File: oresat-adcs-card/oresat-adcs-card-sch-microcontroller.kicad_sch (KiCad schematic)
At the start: 29 parts, among them J2 ORESAT-DEBUG-CONNECTOR-SOLAR, U14 TCAN330GDCNT, U15 STM32F042K6T7, X2 ECS-160-10-36Q-ES-TR

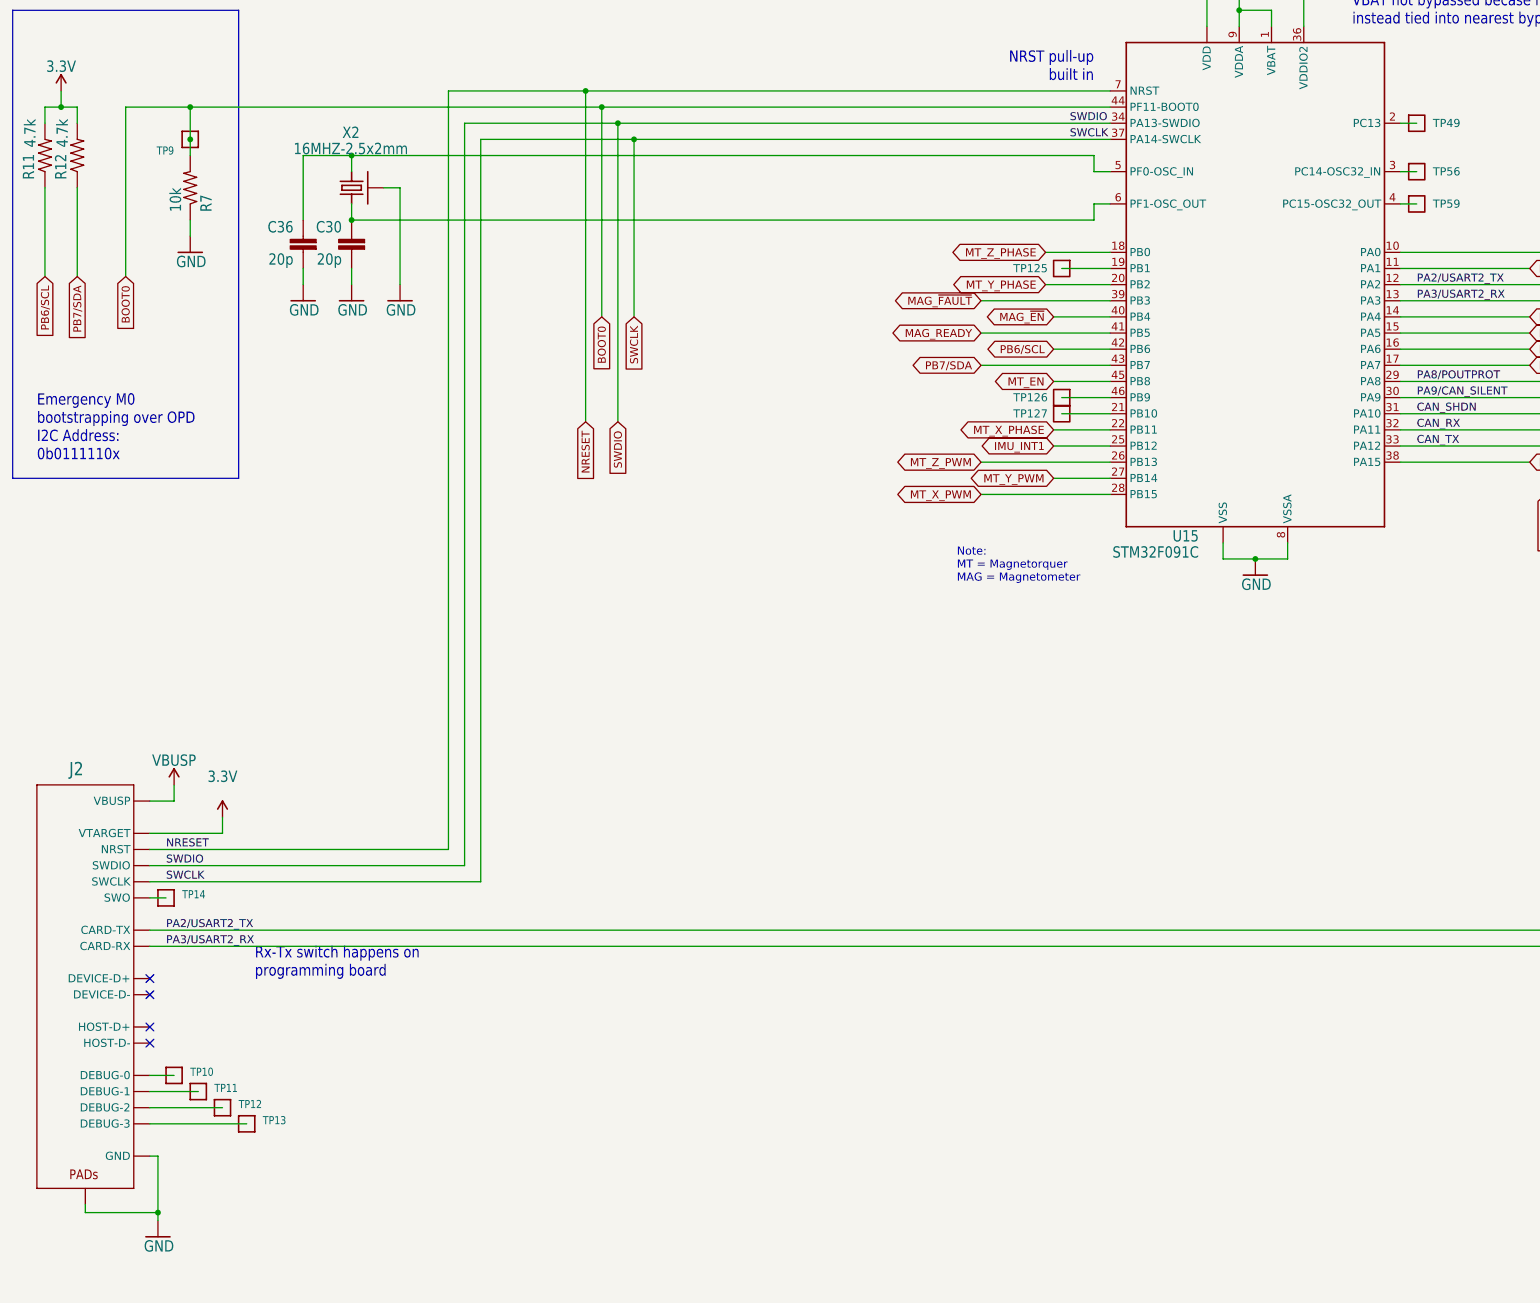
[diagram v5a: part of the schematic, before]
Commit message: Updated ADCS card and fixed library issues
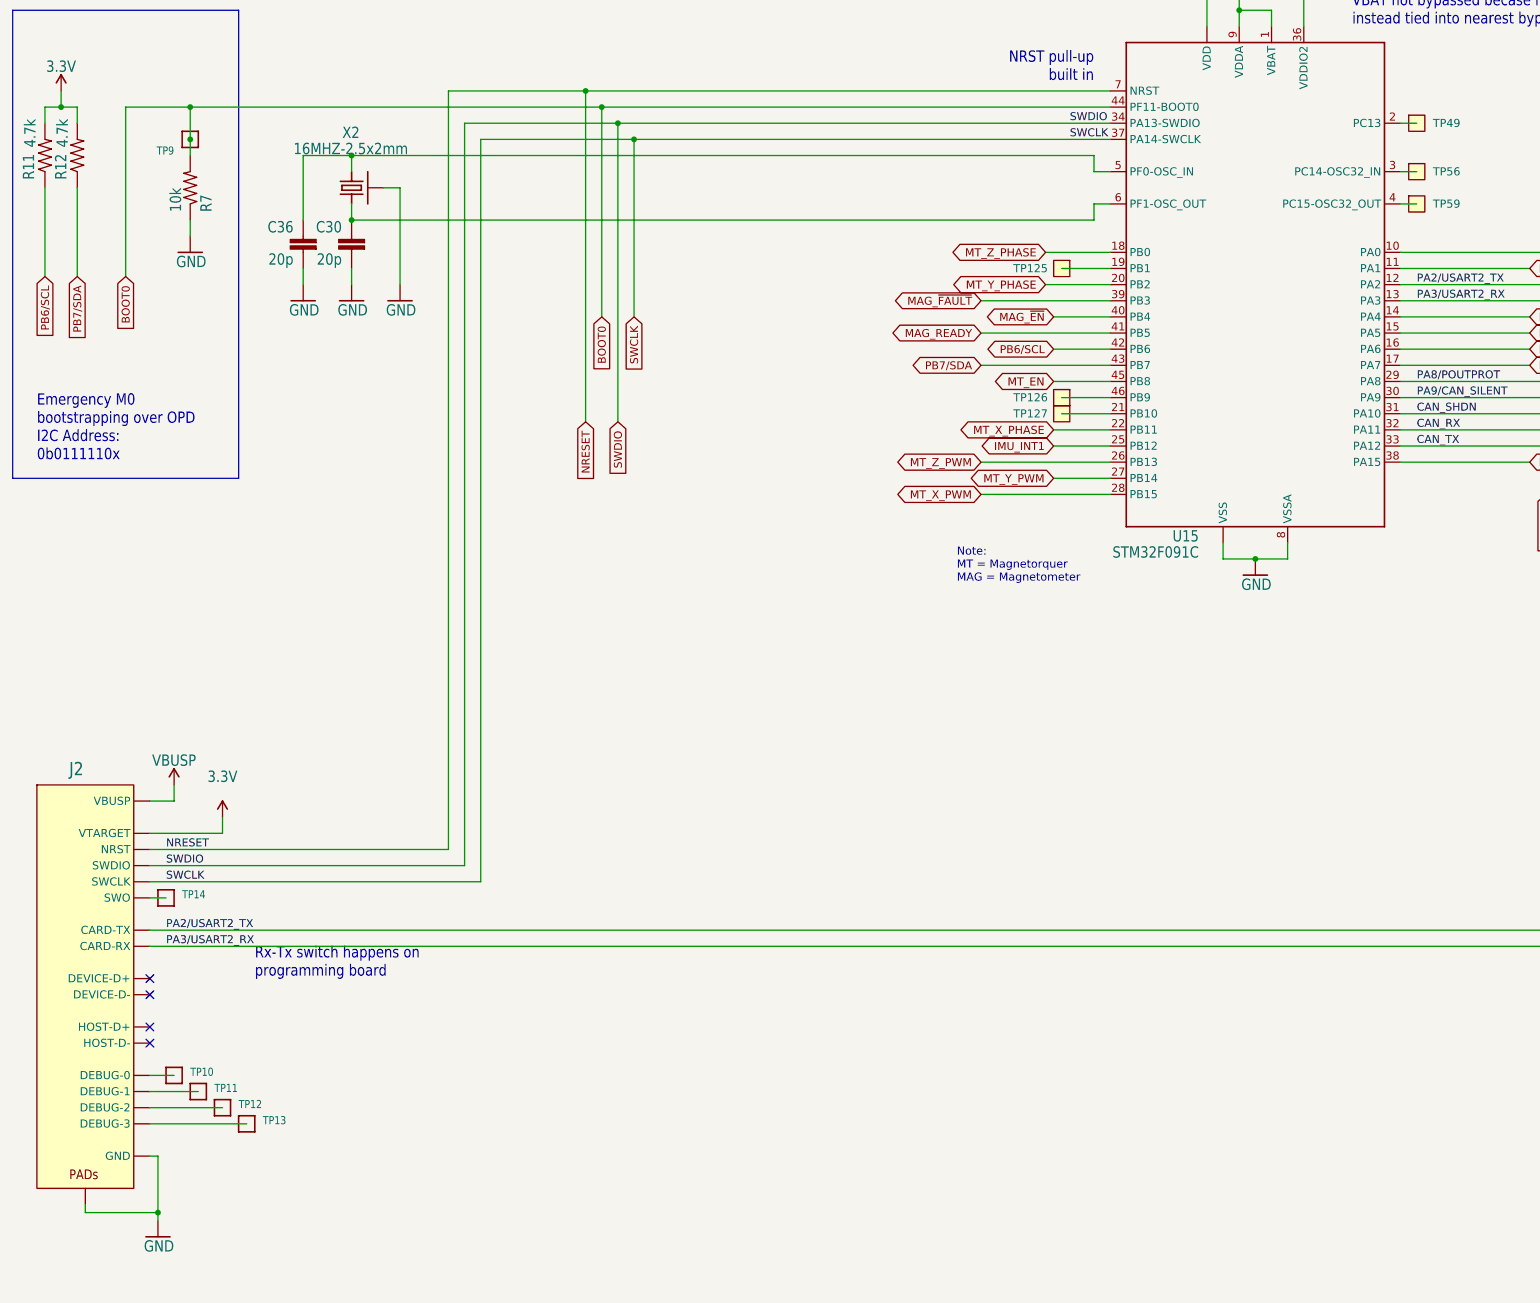
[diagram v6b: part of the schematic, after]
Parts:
- C28, C29, C30, C36, C37, C38, C39, R11, R12, R7, R8, R9: footprint oresat-acs-card:.0603-C-NOSILK -> oresat-passives:0603-C-NOSILK
- J2: footprint oresat-footprints:J-TE_2-1734592-0 -> oresat-connectors:J-TE-2-1734592-0; symbol J-TE-2-1734592-0-oresat-debug-connector:J-TE-Debug-2-1734592-0 -> oresat-connectors:J-TE-2-1734592-0
- TP125, TP126, TP127, TP49, TP56, TP59: footprint OreSat-TestPoint:1X01 -> oresat-misc:TestPoint-0.75mm-th; symbol OreSat-TestPoint:Test-Point -> oresat-misc:Test-Point-0.75mm-th
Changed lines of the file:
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@@
       (effects (font (size 1.778 1.5113)) (justify left bottom))
     )
-    (property "Footprint" "oresat-acs-card:.0603-C-NOSILK" (at 327.66 165.1 0)
+    (property "Footprint" "oresat-passives:0603-C-NOSILK" (at 327.66 165.1 0)
       (effects (font (size 1.27 1.27)) hide)
     )
@@
     )
   )
-  (symbol (lib_id "OreSat-TestPoint:Test-Point") (at 238.76 76.2 0) (unit 1)
+  (symbol (lib_id "oresat-misc:Test-Point-0.75mm-th") (at 238.76 76.2 0) (unit 1)
     (in_bom yes) (on_board yes) (dnp no) (fields_autoplaced)
     (property "Reference" "TP59" (at 241.3 76.1999 0)
@@
       (effects (font (size 1.27 1.27)) hide)
     )
-    (property "Footprint" "OreSat-TestPoint:1X01" (at 238.76 73.66 0)
-      (effects (font (size 1.27 1.27)) hide)
-    )
-    (property "Datasheet" "" (at 238.76 73.66 0)
+    (property "Footprint" "oresat-misc:TestPoint-0.75mm-th" (at 238.76 66.04 0)
+      (effects (font (size 1.27 1.27)) hide)
+    )
+    (property "Datasheet" "" (at 238.76 76.2 0)
       (effects (font (size 1.27 1.27)) hide)
     )
@@
       (effects (font (size 1.778 1.5113)) (justify left bottom))
     )
-    (property "Footprint" "oresat-acs-card:.0603-C-NOSILK" (at 193.04 33.02 0)
+    (property "Footprint" "oresat-passives:0603-C-NOSILK" (at 193.04 33.02 0)
       (effects (font (size 1.27 1.27)) hide)
     )
@@
       (effects (font (size 1.778 1.5113)) (justify left bottom))
     )
-    (property "Footprint" "oresat-acs-card:.0603-C-NOSILK" (at 27.94 68.58 0)
+    (property "Footprint" "oresat-passives:0603-C-NOSILK" (at 27.94 68.58 0)
       (effects (font (size 1.27 1.27)) hide)
     )
@@
     )
   )
-  (symbol (lib_id "OreSat-TestPoint:Test-Point") (at 182.88 109.22 270) (unit 1)
+  (symbol (lib_id "oresat-misc:Test-Point-0.75mm-th") (at 182.88 109.22 270) (unit 1)
     (in_bom yes) (on_board yes) (dnp no)
     (property "Reference" "TP127" (at 175.26 109.22 90)
@@
       (effects (font (size 1.27 1.27)) hide)
     )
-    (property "Footprint" "OreSat-TestPoint:1X01" (at 185.42 109.22 0)
-      (effects (font (size 1.27 1.27)) hide)
-    )
-    (property "Datasheet" "" (at 185.42 109.22 0)
+    (property "Footprint" "oresat-misc:TestPoint-0.75mm-th" (at 193.04 109.22 0)
+      (effects (font (size 1.27 1.27)) hide)
+    )
+    (property "Datasheet" "" (at 182.88 109.22 0)
       (effects (font (size 1.27 1.27)) hide)
     )
@@
       (effects (font (size 1.778 1.5113)) (justify left bottom))
     )
-    (property "Footprint" "oresat-acs-card:.0603-C-NOSILK" (at 226.06 33.02 0)
+    (property "Footprint" "oresat-passives:0603-C-NOSILK" (at 226.06 33.02 0)
       (effects (font (size 1.27 1.27)) hide)
     )
@@
     )
   )
-  (symbol (lib_id "OreSat-TestPoint:Test-Point") (at 182.88 106.68 270) (unit 1)
+  (symbol (lib_id "oresat-misc:Test-Point-0.75mm-th") (at 182.88 106.68 270) (unit 1)
     (in_bom yes) (on_board yes) (dnp no)
     (property "Reference" "TP126" (at 175.26 106.68 90)
@@
       (effects (font (size 1.27 1.27)) hide)
     )
-    (property "Footprint" "OreSat-TestPoint:1X01" (at 185.42 106.68 0)
-      (effects (font (size 1.27 1.27)) hide)
-    )
-    (property "Datasheet" "" (at 185.42 106.68 0)
+    (property "Footprint" "oresat-misc:TestPoint-0.75mm-th" (at 193.04 106.68 0)
+      (effects (font (size 1.27 1.27)) hide)
+    )
+    (property "Datasheet" "" (at 182.88 106.68 0)
       (effects (font (size 1.27 1.27)) hide)
     )
@@
     )
   )
-  (symbol (lib_id "OreSat-TestPoint:Test-Point") (at 238.76 63.5 0) (unit 1)
+  (symbol (lib_id "oresat-misc:Test-Point-0.75mm-th") (at 238.76 63.5 0) (unit 1)
     (in_bom yes) (on_board yes) (dnp no) (fields_autoplaced)
     (property "Reference" "TP49" (at 241.3 63.4999 0)
@@
       (effects (font (size 1.27 1.27)) hide)
     )
-    (property "Footprint" "OreSat-TestPoint:1X01" (at 238.76 60.96 0)
-      (effects (font (size 1.27 1.27)) hide)
-    )
-    (property "Datasheet" "" (at 238.76 60.96 0)
+    (property "Footprint" "oresat-misc:TestPoint-0.75mm-th" (at 238.76 53.34 0)
+      (effects (font (size 1.27 1.27)) hide)
+    )
+    (property "Datasheet" "" (at 238.76 63.5 0)
       (effects (font (size 1.27 1.27)) hide)
     )
@@
     )
   )
-  (symbol (lib_id "OreSat-TestPoint:Test-Point") (at 182.88 86.36 270) (unit 1)
+  (symbol (lib_id "oresat-misc:Test-Point-0.75mm-th") (at 182.88 86.36 270) (unit 1)
     (in_bom yes) (on_board yes) (dnp no)
     (property "Reference" "TP125" (at 175.26 86.36 90)
@@
       (effects (font (size 1.27 1.27)) hide)
     )
-    (property "Footprint" "OreSat-TestPoint:1X01" (at 185.42 86.36 0)
-      (effects (font (size 1.27 1.27)) hide)
-    )
-    (property "Datasheet" "" (at 185.42 86.36 0)
+    (property "Footprint" "oresat-misc:TestPoint-0.75mm-th" (at 193.04 86.36 0)
+      (effects (font (size 1.27 1.27)) hide)
+    )
+    (property "Datasheet" "" (at 182.88 86.36 0)
       (effects (font (size 1.27 1.27)) hide)
     )
@@
       (effects (font (size 1.778 1.5113)) (justify left bottom))
     )
-    (property "Footprint" "oresat-acs-card:.0603-C-NOSILK" (at 71.12 81.28 0)
+    (property "Footprint" "oresat-passives:0603-C-NOSILK" (at 71.12 81.28 0)
       (effects (font (size 1.27 1.27)) hide)
     )
@@
       (effects (font (size 1.778 1.5113)) (justify left bottom))
     )
-    (property "Footprint" "oresat-acs-card:.0603-C-NOSILK" (at 378.46 91.44 0)
+    (property "Footprint" "oresat-passives:0603-C-NOSILK" (at 378.46 91.44 0)
       (effects (font (size 1.27 1.27)) hide)
     )
@@
     )
   )
-  (symbol (lib_id "J-TE-2-1734592-0-oresat-debug-connector:J-TE-Debug-2-1734592-0") (at 29.21 198.12 0) (unit 1)
+  (symbol (lib_id "oresat-connectors:J-TE-2-1734592-0") (at 29.21 198.12 0) (unit 1)
     (in_bom yes) (on_board yes) (dnp no)
     (property "Reference" "J2" (at 26.67 166.37 0)
@@
       (effects (font (size 1.27 1.27)) hide)
     )
-    (property "Footprint" "oresat-footprints:J-TE_2-1734592-0" (at 29.21 189.23 0)
-      (effects (font (size 1.27 1.27)) hide)
-    )
-    (property "Datasheet" "" (at 29.21 189.23 0)
+    (property "Footprint" "oresat-connectors:J-TE-2-1734592-0" (at 29.21 156.21 0)
+      (effects (font (size 1.27 1.27)) hide)
+    )
+    (property "Datasheet" "https://www.te.com/usa-en/product-2-1734592-0.datasheet.pdf" (at 29.21 153.67 0)
       (effects (font (size 1.27 1.27)) hide)
     )
@@
       (effects (font (size 1.778 1.5113)) (justify left bottom))
     )
-    (property "Footprint" "oresat-acs-card:.0603-C-NOSILK" (at 63.5 81.28 0)
+    (property "Footprint" "oresat-passives:0603-C-NOSILK" (at 63.5 81.28 0)
       (effects (font (size 1.27 1.27)) hide)
     )
@@
       (effects (font (size 1.778 1.5113)) (justify left bottom))
     )
-    (property "Footprint" "oresat-acs-card:.0603-C-NOSILK" (at 200.66 33.02 0)
+    (property "Footprint" "oresat-passives:0603-C-NOSILK" (at 200.66 33.02 0)
       (effects (font (size 1.27 1.27)) hide)
     )
@@
       (effects (font (size 1.778 1.5113)) (justify left bottom))
     )
-    (property "Footprint" "oresat-acs-card:.0603-C-NOSILK" (at 45.72 73.66 0)
+    (property "Footprint" "oresat-passives:0603-C-NOSILK" (at 45.72 73.66 0)
       (effects (font (size 1.27 1.27)) hide)
     )
@@
     )
   )
-  (symbol (lib_id "OreSat-TestPoint:Test-Point") (at 238.76 71.12 0) (unit 1)
+  (symbol (lib_id "oresat-misc:Test-Point-0.75mm-th") (at 238.76 71.12 0) (unit 1)
     (in_bom yes) (on_board yes) (dnp no) (fields_autoplaced)
     (property "Reference" "TP56" (at 241.3 71.1199 0)
@@
       (effects (font (size 1.27 1.27)) hide)
     )
-    (property "Footprint" "OreSat-TestPoint:1X01" (at 238.76 68.58 0)
-      (effects (font (size 1.27 1.27)) hide)
-    )
-    (property "Datasheet" "" (at 238.76 68.58 0)
+    (property "Footprint" "oresat-misc:TestPoint-0.75mm-th" (at 238.76 60.96 0)
+      (effects (font (size 1.27 1.27)) hide)
+    )
+    (property "Datasheet" "" (at 238.76 71.12 0)
       (effects (font (size 1.27 1.27)) hide)
     )
@@
       (effects (font (size 1.778 1.5113)) (justify left bottom))
     )
-    (property "Footprint" "oresat-acs-card:.0603-C-NOSILK" (at 22.86 68.58 0)
+    (property "Footprint" "oresat-passives:0603-C-NOSILK" (at 22.86 68.58 0)
       (effects (font (size 1.27 1.27)) hide)
     )
@@
       (effects (font (size 1.778 1.5113)) (justify left bottom))
     )
-    (property "Footprint" "oresat-acs-card:.0603-C-NOSILK" (at 335.28 83.82 0)
+    (property "Footprint" "oresat-passives:0603-C-NOSILK" (at 335.28 83.82 0)
       (effects (font (size 1.27 1.27)) hide)
     )
@@
       (effects (font (size 1.778 1.5113)) (justify left bottom))
     )
-    (property "Footprint" "oresat-acs-card:.0603-C-NOSILK" (at 213.36 33.02 0)
-      (effects (font (size 1.27 1.27)) hide)
-    )
+    (property "Footprint" "oresat-passives:0603-C-NOSILK" (at 213.36 33.02 0)
+      (effects (font (size 1.27 1.27)) hide)
+    )

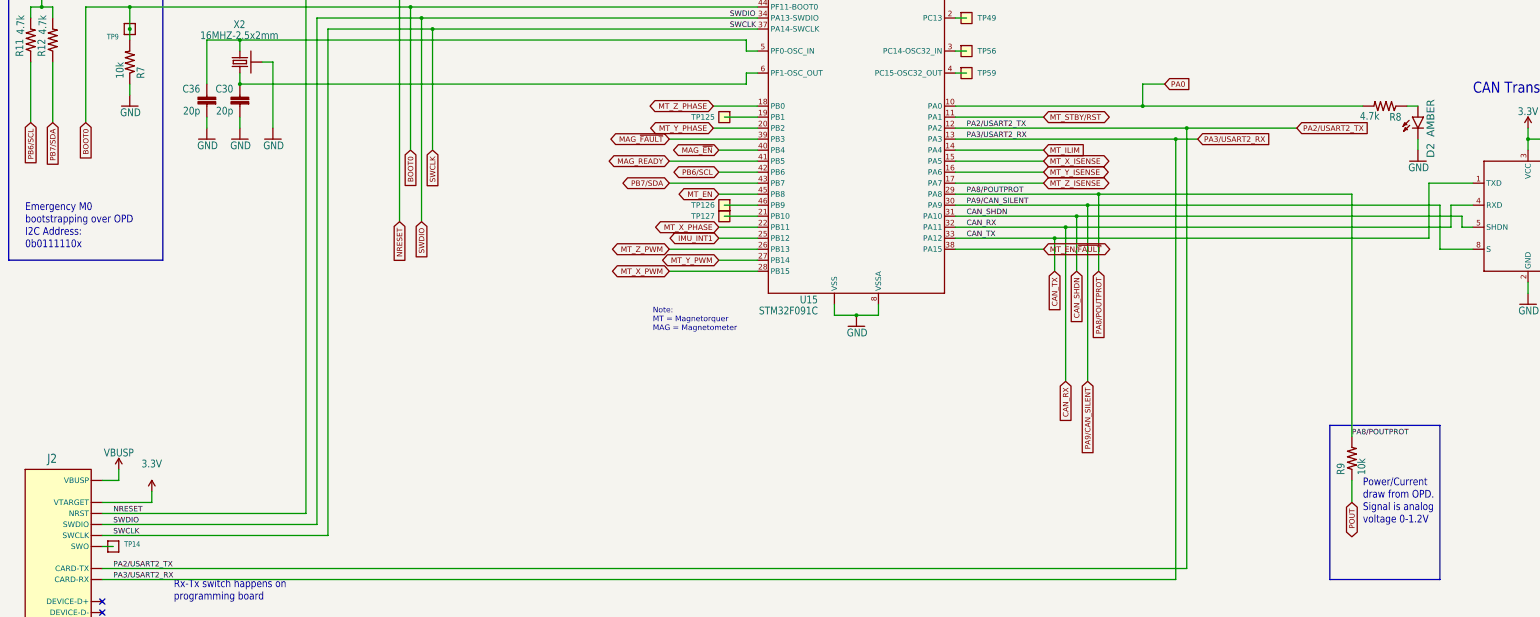
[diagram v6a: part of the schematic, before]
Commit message: Design review changes
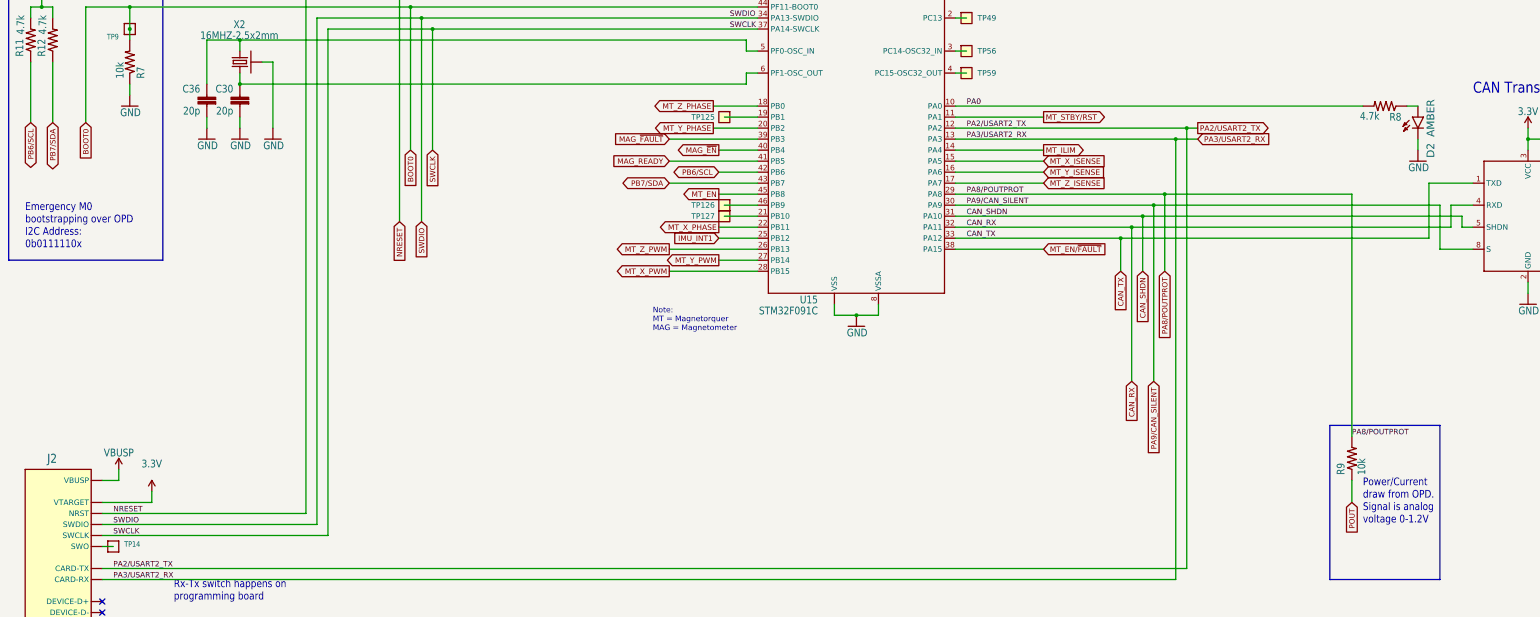
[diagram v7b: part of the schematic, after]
